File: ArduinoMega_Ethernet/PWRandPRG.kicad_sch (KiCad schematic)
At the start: 98 parts, among them J1 RJ45_Amphenol_RJMG1BD3B8K1ANR, J11 Micro_SD_Card_Det_Hirose_DM3AT, J7 EXT_3V3_I2C, J9 PROGRAM_POWER_USBC, U10 TXS0108EPW, U2 CH340C, U3 ISM330DHCX, U4 W5500, U5 AP63205WU, U6 AP63203WU, U7 SE050C2HQ1, U8 AP22804AW5, U9 MCP7940N-xST, Y2 25Mhz, Y3 32.768kHz

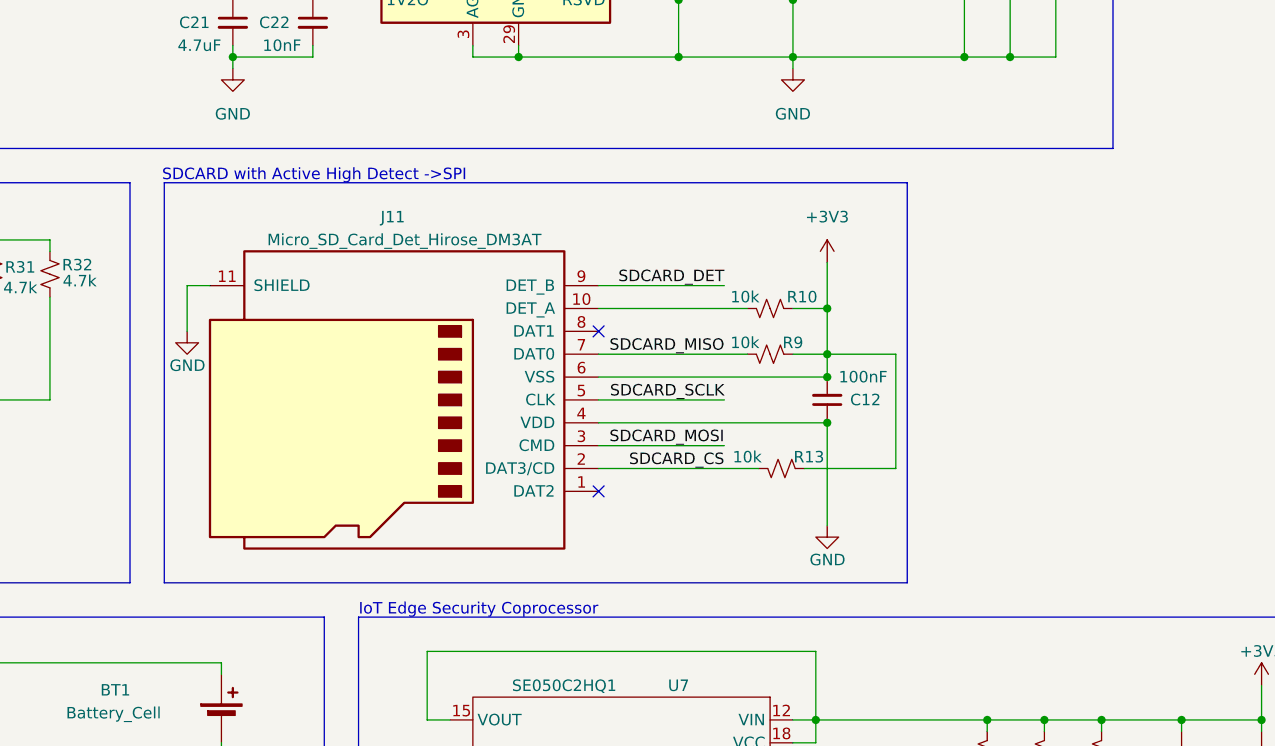
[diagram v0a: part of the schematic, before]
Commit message: swap sd card mosi miso
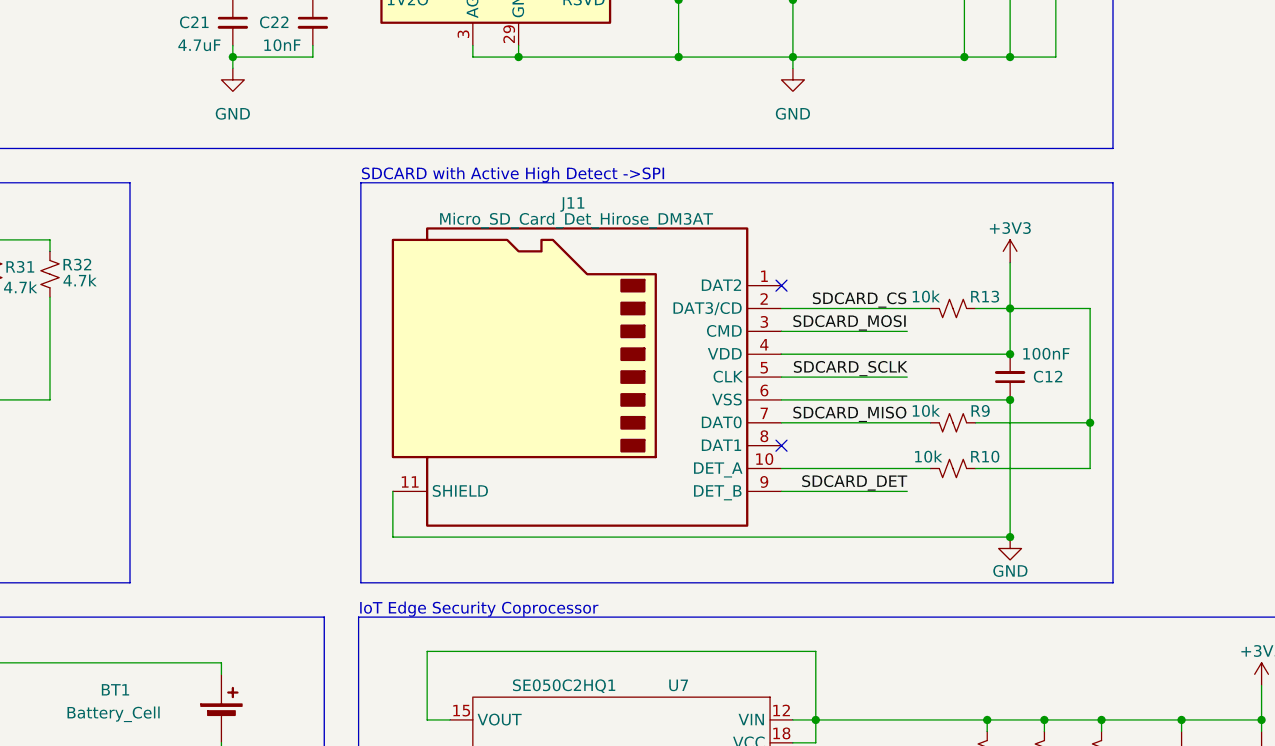
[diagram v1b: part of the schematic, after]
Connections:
- net +3V3: now also J11.4 (VDD); no longer J11.6 (VSS)
- net GND: now also J11.6 (VSS); no longer J11.4 (VDD)
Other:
- moved on the sheet: C12, R10, R13, R9
